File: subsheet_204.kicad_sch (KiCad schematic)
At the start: 10 parts, among them J204 DB-25P Serial Port RS-232, U206 MC1488_QUAD_LINE_EIA-232D_DRI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, U207 MC1489_QUAD_LINE_EIA-232D_REC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

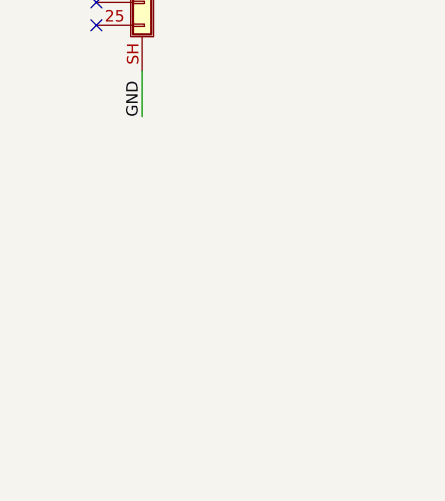
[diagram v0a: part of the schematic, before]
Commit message: add gnd/vcc symbol to start replacing local labels
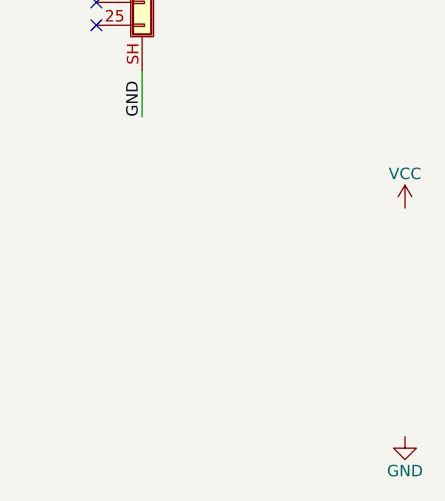
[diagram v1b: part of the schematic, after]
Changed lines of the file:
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@@
     (pin "2")
   )
+  (symbol (lib_id "power:GND") (at 181.61 237.49 0) (unit 1)
+    (in_bom yes) (on_board yes)
+    (property "Reference" "#PWR?" (id 0) (at 181.61 243.84 0)
+      (effects (font (size 1.27 1.27)) hide)
+    )
+    (property "Value" "GND" (id 1) (at 181.61 241.3 0))
+    (property "Footprint" "" (id 2) (at 181.61 237.49 0)
+      (effects (font (size 1.27 1.27)) hide)
+    )
+    (property "Datasheet" "" (id 3) (at 181.61 237.49 0)
+      (effects (font (size 1.27 1.27)) hide)
+    )
+    (pin "1")
+  )
+  (symbol (lib_id "power:VCC") (at 181.61 212.09 0) (unit 1)
+    (in_bom yes) (on_board yes)
+    (property "Reference" "#PWR?" (id 0) (at 181.61 215.9 0)
+      (effects (font (size 1.27 1.27)) hide)
+    )
+    (property "Value" "VCC" (id 1) (at 181.61 208.28 0))
+    (property "Footprint" "" (id 2) (at 181.61 212.09 0)
+      (effects (font (size 1.27 1.27)) hide)
+    )
+    (property "Datasheet" "" (id 3) (at 181.61 212.09 0)
+      (effects (font (size 1.27 1.27)) hide)
+    )
+    (pin "1")
+  )
 )
